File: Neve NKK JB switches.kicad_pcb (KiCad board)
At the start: 2 copper layers, 31 x 35.1 mm, 9 parts

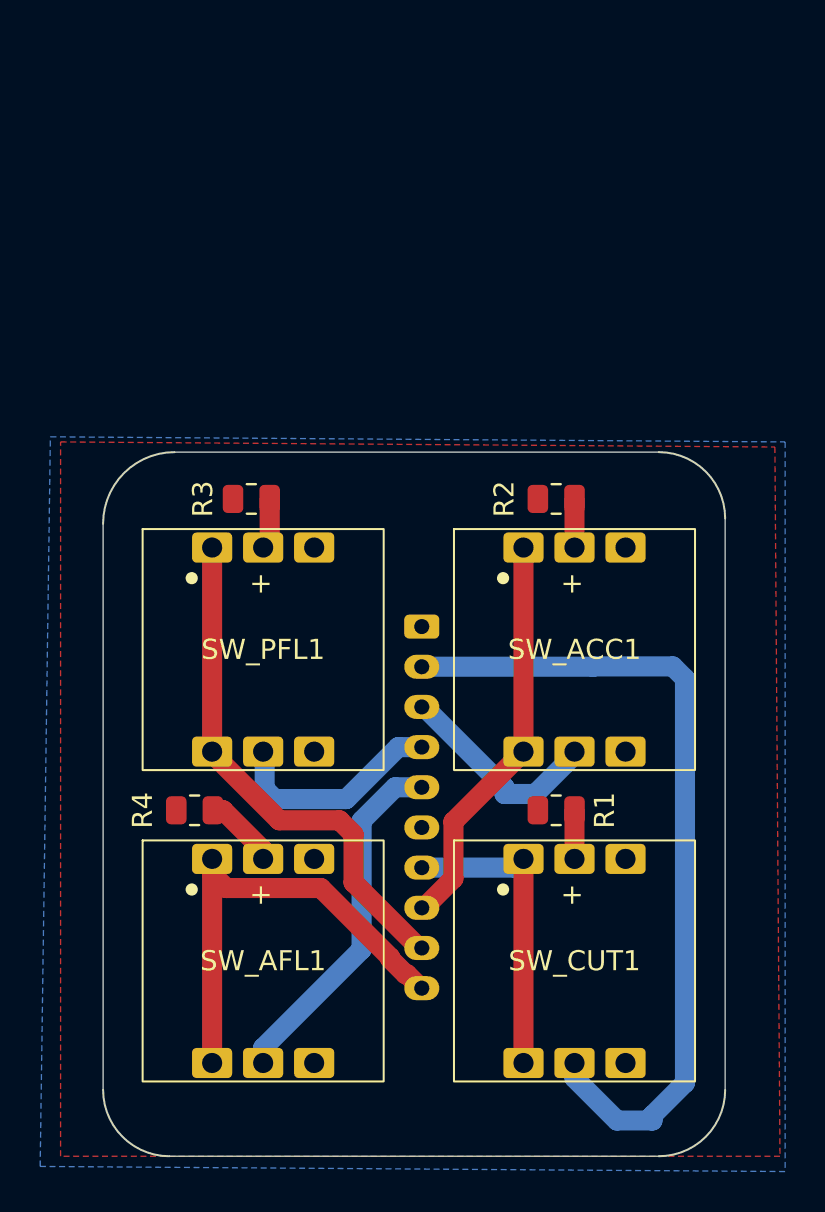
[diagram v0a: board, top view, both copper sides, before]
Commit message: Switched connector
Previous: JST, 1mm pitch
Now: molex 2.54mm pitch
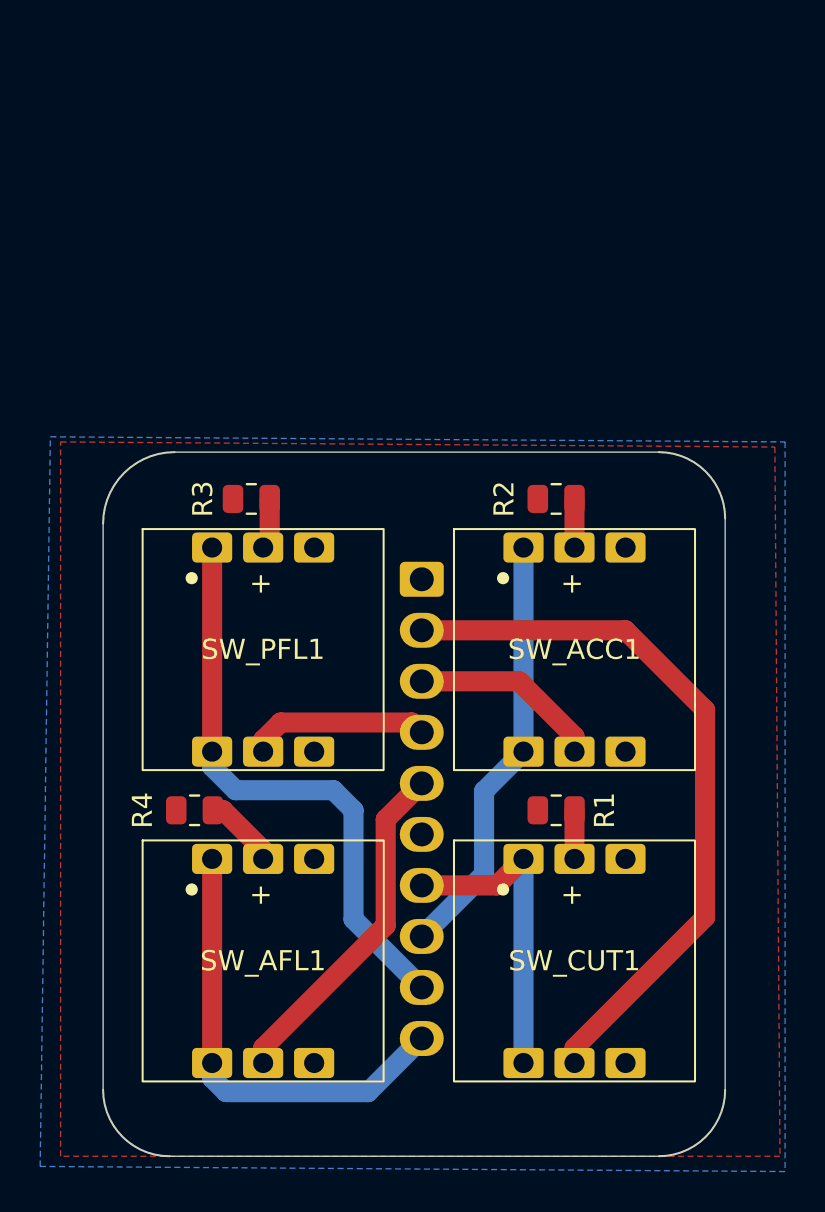
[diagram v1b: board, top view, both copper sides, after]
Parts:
- H1: footprint Connector_JST:JST_PH_B10B-PH-K_1x10_P2.00mm_Vertical -> Connector_Molex:Molex_KK-254_AE-6410-10A_1x10_P2.54mm_Vertical
- moved H1 2.35 mm to (107.9, 96.5)
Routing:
- net Net-(H1-Pin_2): track 41.5 -> 36.0 mm
- net Net-(H1-Pin_9): track 26.1 -> 29.1 mm
- net Net-(H1-Pin_4): track 11.0 -> 9.04 mm
- net Net-(H1-Pin_8): track 20.1 -> 21.5 mm
- net Net-(H1-Pin_3): track 10.6 -> 9.49 mm
- net Net-(H1-Pin_10): track 23.7 -> 22.7 mm
- net Net-(H1-Pin_5): track 17.8 -> 17.2 mm
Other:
- board text added: "V2 - MOLEX 2.54mm rear connector"

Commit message: Movement towards prototype 2
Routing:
- net Net-(H1-Pin_9): track 29.1 -> 32.3 mm
- net Net-(H1-Pin_10): track 22.7 -> 24.3 mm
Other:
- board size 31 x 35.1 mm -> 31 x 49.2 mm
- board text added: "Prototype, not to scale"
- board text added: "V2 - MOLEX 2.54mm rear cnctr Extended top, slot for screw mount"
- board text removed: "V2 - MOLEX 2.54mm rear connector"
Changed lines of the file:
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@@
 		)
+	)
+	(gr_arc
+		(start 96.6 89.6)
+		(mid 95.6 90.6)
+		(end 94.6 89.6)
+		(stroke
+			(width 0.1)
+			(type solid)
+		)
+		(layer "Edge.Cuts")
 	)
 	(gr_line
-		(start 123.000001 93.472)
+		(start 123 79.302)
 		(end 123 121.919999)
 		(stroke
@@
 	)
 	(gr_line
-		(start 95.588867 90.17)
-		(end 119.698001 90.17)
+		(start 95.588866 76)
+		(end 119.698 76)
 		(stroke
 			(width 0.05)
@@
 	)
 	(gr_arc
-		(start 92.032867 93.726)
-		(mid 93.074395 91.211528)
-		(end 95.588867 90.17)
+		(start 92.032866 79.556)
+		(mid 93.074394 77.041528)
+		(end 95.588866 76)
 		(stroke
 			(width 0.1)
@@
 			(width 0.05)
 			(type default)
+		)
+		(layer "Edge.Cuts")
+	)
+	(gr_arc
+		(start 94.6 79.2)
+		(mid 95.6 78.2)
+		(end 96.6 79.2)
+		(stroke
+			(width 0.1)
+			(type solid)
+		)
+		(layer "Edge.Cuts")
+	)
+	(gr_line
+		(start 96.6 79.2)
+		(end 96.6 89.6)
+		(stroke
+			(width 0.1)
+			(type solid)
+		)
+		(layer "Edge.Cuts")
+	)
+	(gr_line
+		(start 94.6 79.2)
+		(end 94.6 89.6)
+		(stroke
+			(width 0.1)
+			(type solid)
 		)
 		(layer "Edge.Cuts")
@@
 	)
 	(gr_line
-		(start 92.032867 93.726)
+		(start 92.032866 79.556)
 		(end 92.032867 121.92)
 		(stroke
@@
 	)
 	(gr_arc
-		(start 119.698001 90.17)
-		(mid 122.032868 91.137133)
-		(end 123.000001 93.472)
+		(start 119.698 76)
+		(mid 122.032867 76.967133)
+		(end 123 79.302)
 		(stroke
 			(width 0.1)
@@
 		(start 123 121.919999)
 		(mid 122.032867 124.254866)
-		(end 119.698 125.221999)
+		(end 119.698 125.222)
 		(stroke
 			(width 0.1)
@@
 		)
 	)
-	(gr_text "V2 - MOLEX 2.54mm rear connector"
-		(at 121.5 123.5 0)
+	(gr_text "V2 - \nMOLEX 2.54mm rear cnctr\nExtended top, \nslot for screw mount"
+		(at 119.697999 79.302 0)
 		(layer "B.SilkS")
 		(effects
@@
 				(thickness 0.1)
 			)
-			(justify left bottom mirror)
+			(justify left top mirror)
+		)
+	)
+	(gr_text "Prototype, not to scale"
+		(at 91.8 70.8 0)
+		(layer "Dwgs.User")
+		(effects
+			(font
+				(size 1 1)
+				(thickness 0.15)
+			)
+			(justify left bottom)
 		)
 	)
 	(dimension
 		(type orthogonal)
-		(layer "User.1")
+		(layer "Dwgs.User")
 		(pts
 			(xy 125.222 107.696) (xy 90.17 107.95)
 		)
-		(height -19.304)
+		(height 25.904)
 		(orientation 0)
 		(format
@@
 		)
 		(gr_text "35.052"
-			(at 107.696 87.242 0)
-			(layer "User.1")
+			(at 107.696 132.45 0)
+			(layer "Dwgs.User")
 			(effects
 				(font
@@
 	(dimension
 		(type orthogonal)
-		(layer "User.1")
+		(layer "Dwgs.User")
 		(pts
 			(xy 87.884 109.982) (xy 128.524 109.982)
 		)
-		(height -25.146)
+		(height 27.018)
 		(orientation 0)
 		(format
@@
 		)
 		(gr_text "40.64"
-			(at 108.204 83.686 0)
-			(layer "User.1")
+			(at 108.204 135.85 0)
+			(layer "Dwgs.User")
 			(effects
 				(font
@@
 		)
 	)
+	(dimension
+		(type orthogonal)
+		(layer "Dwgs.User")
+		(pts
+			(xy 123 121.92) (xy 92.032867 121.92)
+		)
+		(height 7.88)
+		(orientation 0)
+		(format
+			(prefix "")
+			(suffix "")
+			(units 3)
+			(units_format 0)
+			(precision 4)
+			(suppress_zeroes yes)
+		)
+		(style
+			(thickness 0.1)
+			(arrow_length 1.27)
+			(text_position_mode 0)
+			(arrow_direction outward)
+			(extension_height 0.58642)
+			(extension_offset 0.5)
+			(keep_text_aligned yes)
+		)
+		(gr_text "30.9671"
+			(at 107.516433 128.65 0)
+			(layer "Dwgs.User")
+			(effects
+				(font
+					(size 1 1)
+					(thickness 0.15)
+				)
+			)
+		)
+	)
+	(dimension
+		(type orthogonal)
+		(layer "Dwgs.User")
+		(pts
+			(xy 119.698 125.221999) (xy 119.4 75.2)
+		)
+		(height 12.702)
+		(orientation 1)
+		(format
+			(prefix "")
+			(suffix "")
+			(units 3)
+			(units_format 0)
+			(precision 4)
+			(suppress_zeroes yes)
+		)
+		(style
+			(thickness 0.1)
+			(arrow_length 1.27)
+			(text_position_mode 0)
+			(arrow_direction outward)
+			(extension_height 0.58642)
+			(extension_offset 0.5)
+			(keep_text_aligned yes)
+		)
+		(gr_text "50.022"
+			(at 131.25 100.210999 90)
+			(layer "Dwgs.User")
+			(effects
+				(font
+					(size 1 1)
+					(thickness 0.15)
+				)
+			)
+		)
+	)
 	(segment
 		(start 112.75 101.58)
@@
 	)
 	(segment
-		(start 98.161 122.031)
-		(end 97.46 121.33)
-		(width 1)
-		(layer "B.Cu")
-		(net 2)
-	)
-	(segment
-		(start 105.226082 122.031)
-		(end 98.161 122.031)
-		(width 1)
-		(layer "B.Cu")
-		(net 2)
-	)
-	(segment
 		(start 97.46 121.33)
 		(end 97.46 120.58)
@@
 	)
 	(segment
+		(start 105 123.2)
+		(end 99.33 123.2)
+		(width 1)
+		(layer "B.Cu")
+		(net 2)
+	)
+	(segment
+		(start 99.33 123.2)
+		(end 97.46 121.33)
+		(width 1)
+		(layer "B.Cu")
+		(net 2)
+	)
+	(segment
 		(start 107.897082 119.36)
-		(end 105.226082 122.031)
+		(end 107.897082 120.302918)
 		(width 1)
 		(layer "B.Cu")
 		(net 2)
+	)
+	(segment
+		(start 107.897082 120.302918)
+		(end 105 123.2)
+		(width 1)
+		(layer "B.Cu")
+		(net 2)
+	)
+	(segment
+		(start 106.101082 108.456)
+		(end 106.101082 113.728918)
+		(width 1)
+		(layer "F.Cu")
+		(net 3)
+	)
+	(segment
+		(start 107.897082 106.66)
+		(end 106.101082 108.456)
+		(width 1)
+		(layer "F.Cu")
+		(net 3)
 	)
 	(segment
@@
 	)
 	(segment
-		(start 107.897082 106.66)
-		(end 106.101082 108.456)
-		(width 1)
-		(layer "F.Cu")
-		(net 3)
-	)
-	(segment
-		(start 106.101082 108.456)
-		(end 106.101082 113.728918)
-		(width 1)
-		(layer "F.Cu")
-		(net 3)
-	)
-	(segment
 		(start 106.101082 113.728918)
 		(end 100 119.83)
@@
 	)
 	(segment
+		(start 107.406082 103.629)
+		(end 100.871 103.629)
+		(width 1)
+		(layer "F.Cu")
+		(net 4)
+	)
+	(segment
+		(start 100.871 103.629)
+		(end 100 104.5)
+		(width 1)
+		(layer "F.Cu")
+		(net 4)
+	)
+	(segment
 		(start 107.897082 104.12)
 		(end 107.406082 103.629)
@@
 	)
 	(segment
-		(start 100.871 103.629)
-		(end 100 104.5)
-		(width 1)
-		(layer "F.Cu")
-		(net 4)
-	)
-	(segment
-		(start 107.406082 103.629)
-		(end 100.871 103.629)
-		(width 1)
-		(layer "F.Cu")
-		(net 4)
-	)
-	(segment
 		(start 111.64 111.74)
 		(end 112.96 110.42)
@@
 	)
 	(segment
-		(start 103.5 107)
-		(end 98.63 107)
+		(start 95.4 107.14)
+		(end 95.4 111.8)
 		(width 1)
 		(layer "B.Cu")
@@
 	)
 	(segment
-		(start 104.5 113.422918)
-		(end 104.5 108)
+		(start 95.4 111.8)
+		(end 100.42 116.82)
 		(width 1)
 		(layer "B.Cu")
@@
 	)
 	(segment
-		(start 104.5 108)
-		(end 103.5 107)
+		(start 97.46 105.08)
+		(end 95.4 107.14)
 		(width 1)
 		(layer "B.Cu")
@@
 	)
 	(segment
-		(start 107.897082 116.82)
-		(end 104.5 113.422918)
-		(width 1)
-		(layer "B.Cu")
-		(net 7)
-	)
-	(segment
-		(start 98.63 107)
-		(end 97.46 105.83)
-		(width 1)
-		(layer "B.Cu")
-		(net 7)
-	)
-	(segment
-		(start 97.46 105.83)
-		(end 97.46 105.08)
+		(start 100.42 116.82)
+		(end 107.897082 116.82)
 		(width 1)
 		(layer "B.Cu")
@@
 		(polygon
 			(pts
-				(xy 89.916 89.662) (xy 125.476 89.916) (xy 125.73 125.222) (xy 89.916 125.222)
+				(xy 90.116 73.662) (xy 125.676 73.916) (xy 125.73 125.222) (xy 89.916 125.222)
 			)
 		)
@@
 		(polygon
 			(pts
-				(xy 89.408 89.408) (xy 125.984 89.662) (xy 125.984 125.984) (xy 88.9 125.73)
-			)
-		)
+				(xy 89.408 73.808) (xy 125.984 74.062) (xy 125.984 125.984) (xy 88.9 125.73)
+			)
+		)

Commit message: work towards prototype 2
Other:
- board size 31 x 49.2 mm -> 29.9 x 52.3 mm
- board text added: "Button cap"
- board text added: "Button to base of cap"
- board text added: "PCB"
- board text added: "Pin spacer:"
- board text added: "Side view: PCB spacing"
- board text added: "back of faceplate"
- board text added: "https://www.mouser.co.uk/ProductDetail/Mill-Max/316-43-103-41-006000?qs=s8Nb1z4Wn%2FREOM5qHB9aiQ%3D%3D"
- board text removed: "Prototype, not to scale"
